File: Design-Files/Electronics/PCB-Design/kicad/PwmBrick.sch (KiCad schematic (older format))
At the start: 51 parts, among them J1 Conn_01x02, J2 USB_B_Micro, J3 Conn_01x02, J4 Conn_01x06_Male, Q1 Q_NMOS_DGS, Q2 Q_NMOS_DGS, SW1 SW_Push, SW2 SW_Push, U1 MAX5026, U2 MCP1700-2502E_SOT89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

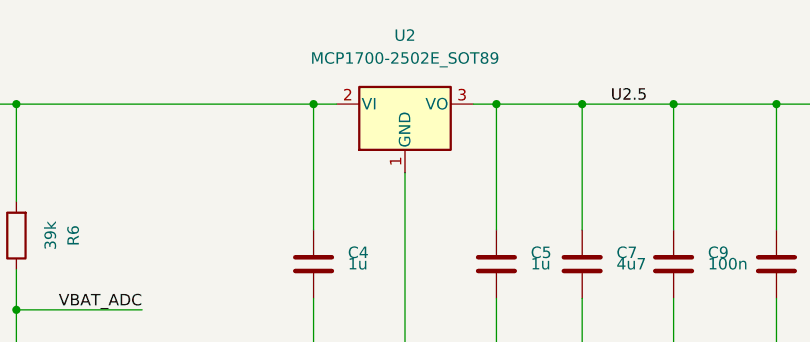
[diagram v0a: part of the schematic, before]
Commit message: Changed the LDO for the microcontroller from the old 2.5V to the new 3.3V
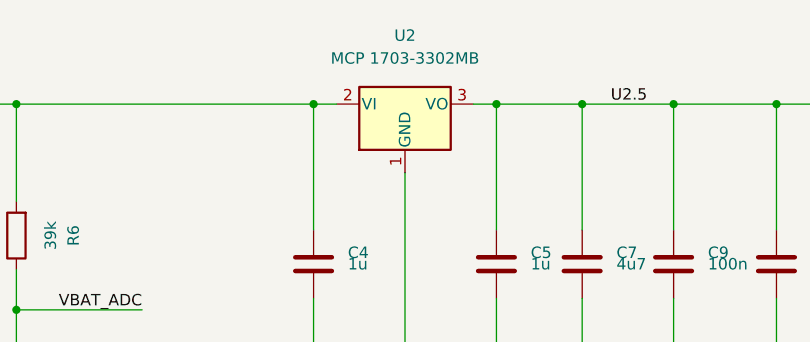
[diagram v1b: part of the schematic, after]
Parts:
- U2: value MCP1700-2502E_SOT89 -> MCP 1703-3302MB
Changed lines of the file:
@@
 P 3725 1100
 F 0 "U2" H 3725 1400 50  0000 C CNN
-F 1 "MCP1700-2502E_SOT89" H 3725 1300 50  0000 C CNN
+F 1 "MCP 1703-3302MB" H 3725 1300 50  0000 C CNN
 F 2 "Package_TO_SOT_SMD:SOT-89-3" H 3725 1300 50  0001 C CNN
 F 3 "http://ww1.microchip.com/downloads/en/DeviceDoc/20001826D.pdf" H 3725 1050 50  0001 C CNN
